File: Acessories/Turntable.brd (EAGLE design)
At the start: 80 x 50 mm, 28 parts, among them J1 HEADER4, M1 ARDUINO-NANO-3.0, U2 A4988, X1 MKDSN1,5/4-5,08

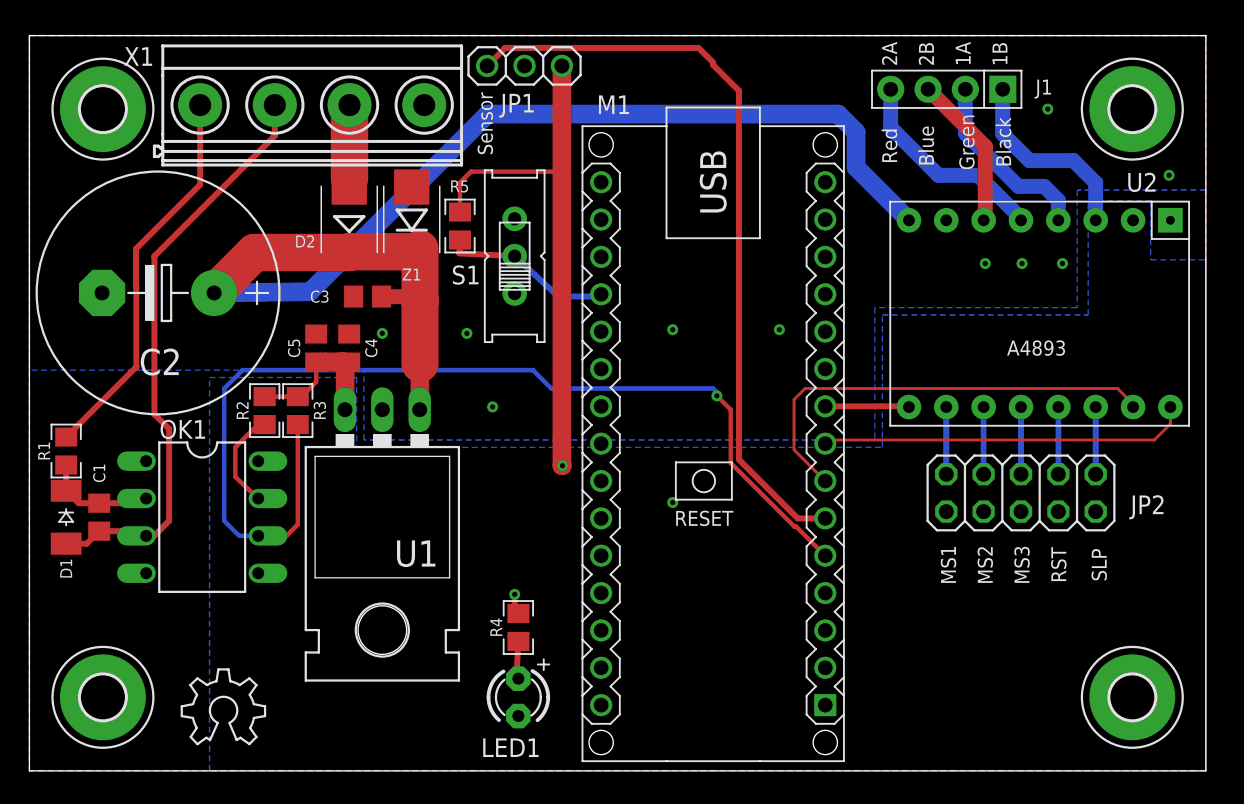
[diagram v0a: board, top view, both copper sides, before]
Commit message: Add files via upload
Added 12V regulator, Address label
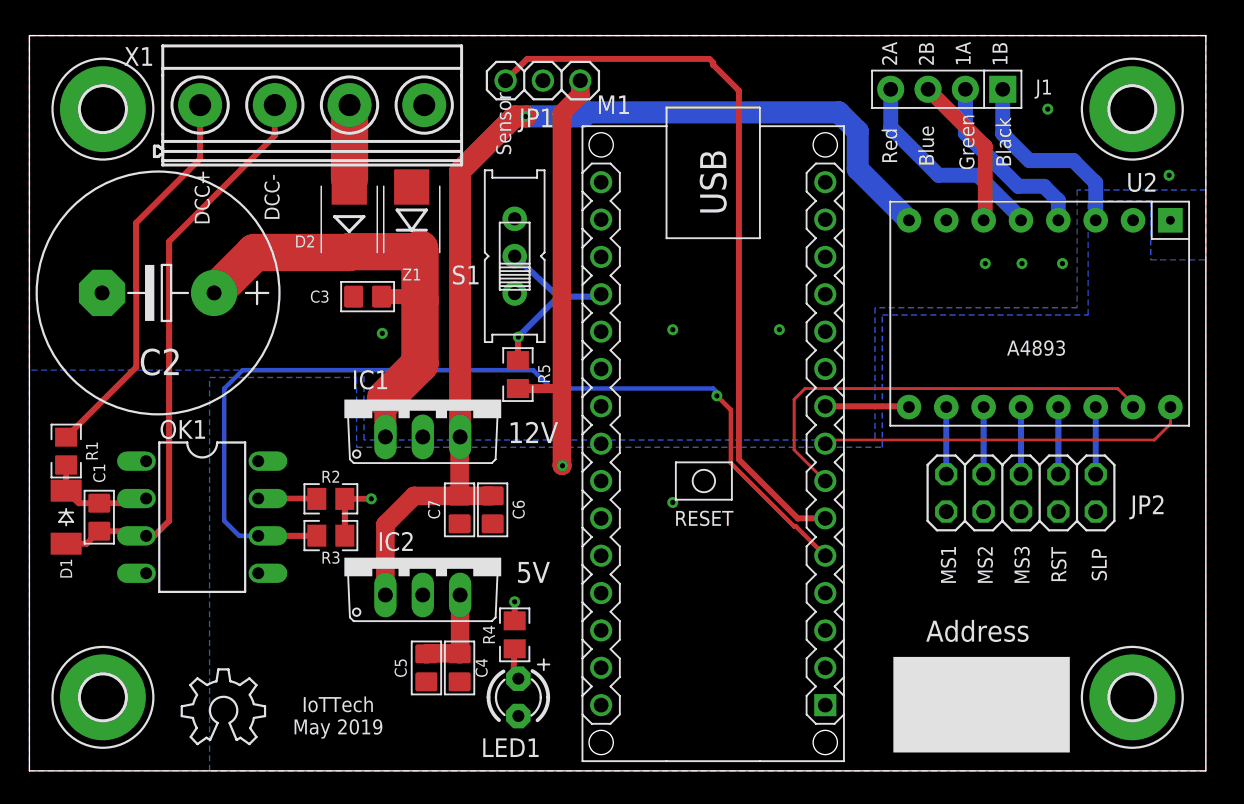
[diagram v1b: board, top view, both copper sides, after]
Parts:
- removed U1: (no value), SparkFun-IC-Power:TO-220-ALT
- added C6: 10uF, GJR:0805
- added C7: 0.1uF, GJR:0805
- added IC1: 7812TV, linear:TO220V
- added IC2: 7805TV, linear:TO220V
- C1, C3, C4, C5: device rcl:C0805 -> GJR:0805
- moved C4 23.0 mm to (-10.8, -18.0), turned to 270 degrees
- moved C5 23.0 mm to (-13.0, -18.0), turned to 270 degrees
- moved R5 10.8 mm to (-6.78, 1.95), turned to 270 degrees
- moved R3 8.79 mm to (-19.5, -9.00), turned to 0 degrees
- moved R2 7.50 mm to (-19.5, -6.50), turned to 0 degrees
- moved JP1 1.60 mm to (-5.08, 21.9)
- moved R4 0.56 mm to (-7.00, -15.8)
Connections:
- new net +12V: C6.1, C7.1, IC1.3, IC2.1, U2.8
- net +15V: now also IC1.1; no longer U1.IN, U2.8
- net +5V: now also IC2.3; no longer U1.OUT
- net GND: now also C6.2, C7.2, IC1.2, IC2.2; no longer U1.GND
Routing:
- net +12V: track 0.00 -> 71.7 mm, vias 0 -> 1
- net +15V: track 84.9 -> 31.7 mm
- net +5V: track 49.2 -> 41.9 mm, vias 2 -> 3
- net DCCIN: track 70.4 -> 64.6 mm
- net N$4: track 6.80 -> 4.00 mm
- net POS: track 51.5 -> 50.1 mm
- net TRACK2: track 40.0 -> 39.1 mm
- net LEARN: track 11.7 -> 12.5 mm, vias 0 -> 1
- net N$1: track 5.02 -> 5.58 mm
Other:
- board text added: "12V"
- board text added: "5V"
- board text added: "Address"
- board text added: "DCC+"
- board text added: "DCC-"
- board text added: "IoTTech May 2019"

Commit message: Add files via upload
Minor tweaks
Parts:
- moved R4 0.25 mm to (-6.75, -15.8)
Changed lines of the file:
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@@
 <wire x1="40" y1="25" x2="-40" y2="25" width="0" layer="20"/>
 <wire x1="-40" y1="25" x2="-40" y2="-25" width="0" layer="20"/>
-<text x="-7.75" y="19" size="1.016" layer="21" rot="R90" align="center">Sensor</text>
+<text x="-9.75" y="22" size="1.016" layer="21" rot="R90" align="center">Sensor</text>
 <text x="18.5" y="23.75" size="1.016" layer="21" rot="R90" align="center">2A</text>
 <text x="21" y="23.75" size="1.016" layer="21" rot="R90" align="center">2B</text>
@@
 <attribute name="VALUE" x="-19.5" y="-10.5" size="0.8128" layer="27" align="center"/>
 </element>
-<element name="R4" library="rcl" package="R0805" value="470R" x="-7" y="-15.75" smashed="yes" rot="R90">
-<attribute name="NAME" x="-8.75" y="-15.75" size="0.8128" layer="25" rot="R90" align="center"/>
-<attribute name="VALUE" x="-5.5" y="-15.75" size="0.6096" layer="27" rot="R90" align="center"/>
+<element name="R4" library="rcl" package="R0805" value="470R" x="-6.75" y="-15.75" smashed="yes" rot="R90">
+<attribute name="NAME" x="-8.5" y="-15.75" size="0.8128" layer="25" rot="R90" align="center"/>
+<attribute name="VALUE" x="-5.25" y="-15.75" size="0.6096" layer="27" rot="R90" align="center"/>
 </element>
 <element name="R1" library="rcl" package="R0805" value="1K" x="-37.5" y="-3.25" smashed="yes" rot="R90">
@@
 <vertex x="-40" y="2.25"/>
 </polygon>
-<via x="-8.5" y="-0.25" extent="1-16" drill="0.35"/>
+<via x="-6.75" y="-1" extent="1-16" drill="0.35"/>
 <via x="3.75" y="5" extent="1-16" drill="0.35"/>
 <via x="11" y="5" extent="1-16" drill="0.35"/>
@@
 <vertex x="-27.75" y="-25"/>
 </polygon>
-<wire x1="-7" y1="-13.5" x2="-7" y2="-14.8" width="0.4064" layer="1"/>
-<via x="-7" y="-13.5" extent="1-16" drill="0.35"/>
+<wire x1="-6.75" y1="-13.5" x2="-6.75" y2="-14.8" width="0.4064" layer="1"/>
+<via x="-6.75" y="-13.5" extent="1-16" drill="0.35"/>
 <wire x1="-3.75" y1="-4" x2="-3.75" y2="-4.25" width="0.4064" layer="1"/>
 <via x="-3.75" y="-4.25" extent="1-16" drill="0.35"/>
@@
 <contactref element="R4" pad="1"/>
 <contactref element="LED1" pad="A"/>
-<wire x1="-6.75" y1="-18.73" x2="-7.096403125" y2="-18.516828125" width="0.4064" layer="1"/>
-<wire x1="-7.096403125" y1="-18.516828125" x2="-7" y2="-16.7" width="0.4064" layer="1"/>
+<wire x1="-6.75" y1="-18.73" x2="-6.75" y2="-16.7" width="0.4064" layer="1"/>
 </signal>
 <signal name="+15V">

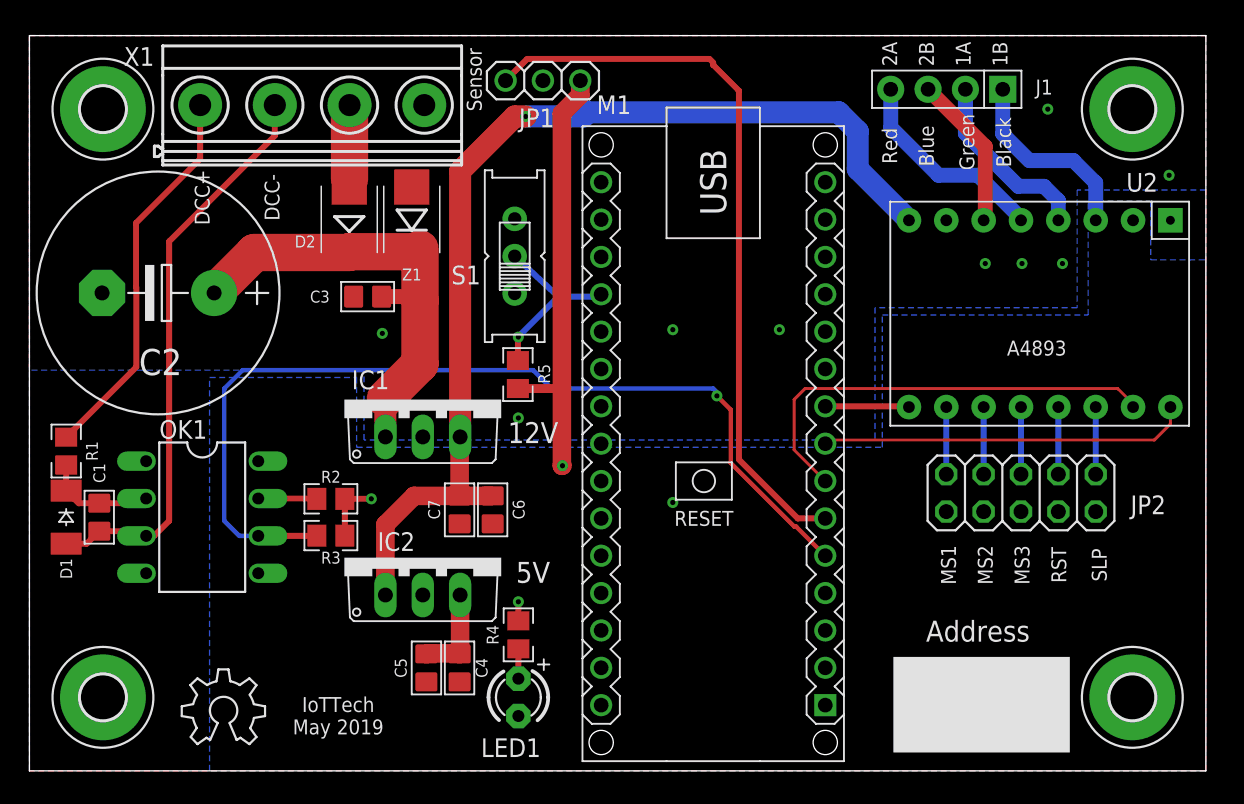
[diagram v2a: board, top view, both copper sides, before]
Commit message: Add files via upload
Added GPIO control of the stepper motor board settings, updated Peco turntable build instructions.
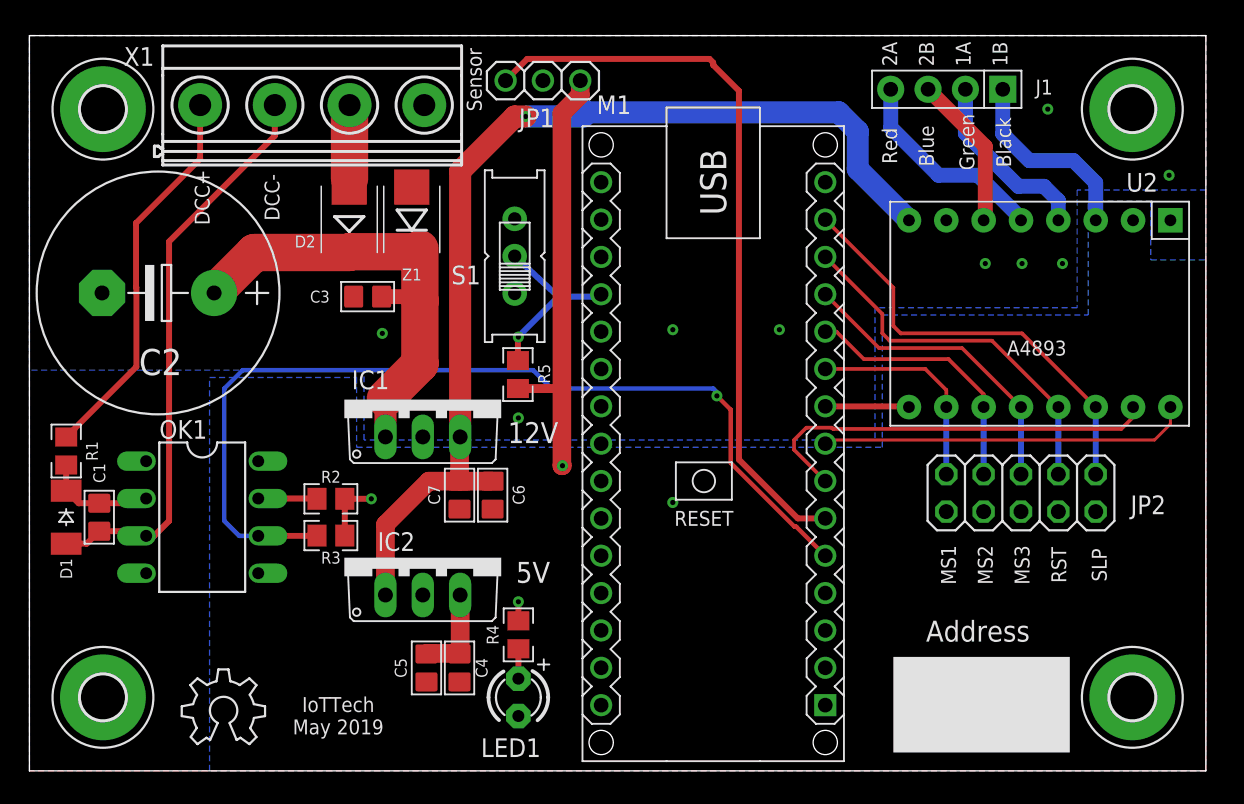
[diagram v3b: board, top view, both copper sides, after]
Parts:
- moved C6 1.00 mm to (-8.50, -6.25)
- moved C7 1.00 mm to (-10.8, -6.25)
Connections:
- net BLACK renamed 1B
- net BLUE renamed 2B
- net GREEN renamed 1A
- net RED renamed 2A
- removed net N$11: JP2.9, U2.10
- removed net N$12: JP2.1, U2.14
- removed net N$13: JP2.3, U2.13
- removed net N$14: JP2.5, U2.12
- removed net N$15: JP2.7, U2.11
- new net !RESET: JP2.3, M1.J1.13, U2.13
- new net !SLEEP: JP2.1, M1.J1.14, U2.14
- new net MS1: JP2.9, M1.J1.10, U2.10
- new net MS2: JP2.7, M1.J1.11, U2.11
- new net MS3: JP2.5, M1.J1.12, U2.12
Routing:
- net !SLEEP: track 0.00 -> 29.8 mm
- net !RESET: track 0.00 -> 25.4 mm
- net MS3: track 0.00 -> 21.1 mm
- net MS2: track 0.00 -> 18.0 mm
- net MS1: track 0.00 -> 14.6 mm
- net N$15: track 4.57 -> 0.00 mm
- net N$14: track 4.57 -> 0.00 mm
- net N$13: track 4.57 -> 0.00 mm
- net N$12: track 4.57 -> 0.00 mm
- net N$11: track 4.57 -> 0.00 mm
- net STEP: track 30.4 -> 28.1 mm
- net +12V: track 71.7 -> 71.1 mm
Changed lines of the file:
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@@
 <attribute name="VALUE" x="-8.28" y="1.95" size="0.6096" layer="27" rot="R270" align="center"/>
 </element>
-<element name="C6" library="GJR" package="0805" value="10uF" x="-8.5" y="-7.25" smashed="yes" rot="R270">
-<attribute name="FARNELL" value="" x="-8.5" y="-7.25" size="1.778" layer="27" rot="R270" display="off"/>
-<attribute name="MANUFACTURER" value="" x="-8.5" y="-7.25" size="1.778" layer="27" rot="R270" display="off"/>
-<attribute name="NAME" x="-6.73" y="-7.23" size="0.8128" layer="25" rot="R270" align="center"/>
-<attribute name="PARTNUMBER" value="" x="-8.5" y="-7.25" size="1.778" layer="27" rot="R270" display="off"/>
-<attribute name="VALUE" x="-11.04" y="-5.98" size="1.27" layer="27" rot="R270"/>
-</element>
-<element name="C7" library="GJR" package="0805" value="0.1uF" x="-10.75" y="-7.25" smashed="yes" rot="R270">
-<attribute name="FARNELL" value="" x="-10.75" y="-7.25" size="1.778" layer="27" rot="R270" display="off"/>
-<attribute name="MANUFACTURER" value="" x="-10.75" y="-7.25" size="1.778" layer="27" rot="R270" display="off"/>
-<attribute name="NAME" x="-12.48" y="-7.23" size="0.8128" layer="25" rot="R270" align="center"/>
-<attribute name="PARTNUMBER" value="" x="-10.75" y="-7.25" size="1.778" layer="27" rot="R270" display="off"/>
-<attribute name="VALUE" x="-13.29" y="-5.98" size="1.27" layer="27" rot="R270"/>
+<element name="C6" library="GJR" package="0805" value="10uF" x="-8.5" y="-6.25" smashed="yes" rot="R270">
+<attribute name="FARNELL" value="" x="-8.5" y="-6.25" size="1.778" layer="27" rot="R270" display="off"/>
+<attribute name="MANUFACTURER" value="" x="-8.5" y="-6.25" size="1.778" layer="27" rot="R270" display="off"/>
+<attribute name="NAME" x="-6.73" y="-6.23" size="0.8128" layer="25" rot="R270" align="center"/>
+<attribute name="PARTNUMBER" value="" x="-8.5" y="-6.25" size="1.778" layer="27" rot="R270" display="off"/>
+<attribute name="VALUE" x="-11.04" y="-4.98" size="1.27" layer="27" rot="R270"/>
+</element>
+<element name="C7" library="GJR" package="0805" value="0.1uF" x="-10.75" y="-6.25" smashed="yes" rot="R270">
+<attribute name="FARNELL" value="" x="-10.75" y="-6.25" size="1.778" layer="27" rot="R270" display="off"/>
+<attribute name="MANUFACTURER" value="" x="-10.75" y="-6.25" size="1.778" layer="27" rot="R270" display="off"/>
+<attribute name="NAME" x="-12.48" y="-6.23" size="0.8128" layer="25" rot="R270" align="center"/>
+<attribute name="PARTNUMBER" value="" x="-10.75" y="-6.25" size="1.778" layer="27" rot="R270" display="off"/>
+<attribute name="VALUE" x="-13.29" y="-4.98" size="1.27" layer="27" rot="R270"/>
 </element>
 <element name="IC1" library="linear" library_urn="urn:adsk.eagle:library:262" package="TO220V" package3d_urn="urn:adsk.eagle:package:16417/2" value="7812TV" x="-13.25" y="0.25" smashed="yes">
@@
 <wire x1="-18.2311" y1="14.7189" x2="-18.2311" y2="15.25" width="1.016" layer="1"/>
 </signal>
-<signal name="BLACK">
+<signal name="1B">
 <contactref element="U2" pad="3"/>
 <contactref element="J1" pad="1"/>
@@
 <wire x1="26.19" y1="18.31" x2="28" y2="16.5" width="1.016" layer="16"/>
 </signal>
-<signal name="GREEN">
+<signal name="1A">
 <contactref element="U2" pad="4"/>
 <contactref element="J1" pad="2"/>
@@
 <wire x1="23.65" y1="21.35" x2="23.65" y2="18.35" width="1.016" layer="16"/>
 </signal>
-<signal name="RED">
+<signal name="2A">
 <contactref element="U2" pad="5"/>
 <contactref element="J1" pad="4"/>
@@
 <wire x1="27.43" y1="12.57" x2="27.43" y2="12.44" width="1.016" layer="16"/>
 </signal>
-<signal name="BLUE">
+<signal name="2B">
 <contactref element="U2" pad="6"/>
 <contactref element="J1" pad="3"/>
@@
 <contactref element="M1" pad="J1.7"/>
 <contactref element="U2" pad="15"/>
-<wire x1="14.12" y1="-5.29" x2="12" y2="-3.17" width="0.2032" layer="1"/>
-<wire x1="12" y1="-3.17" x2="12" y2="0.25" width="0.2032" layer="1"/>
-<wire x1="12" y1="0.25" x2="12.75" y2="1" width="0.2032" layer="1"/>
-<wire x1="12.75" y1="1" x2="34" y2="1" width="0.2032" layer="1"/>
-<wire x1="34" y1="1" x2="35.05" y2="-0.05" width="0.2032" layer="1"/>
-<wire x1="35.05" y1="-0.05" x2="35.05" y2="-0.26" width="0.2032" layer="1"/>
+<wire x1="14.12" y1="-5.29" x2="12" y2="-3.17" width="0.254" layer="1"/>
+<wire x1="12" y1="-3.17" x2="12" y2="-2.5" width="0.254" layer="1"/>
+<wire x1="14.56909375" y1="-1.6658" x2="14.65329375" y2="-1.75" width="0.254" layer="1"/>
+<wire x1="14.65329375" y1="-1.75" x2="34.25" y2="-1.75" width="0.254" layer="1"/>
+<wire x1="12.8342" y1="-1.6658" x2="14.56909375" y2="-1.6658" width="0.254" layer="1"/>
+<wire x1="34.25" y1="-1.75" x2="35.05" y2="-0.95" width="0.254" layer="1"/>
+<wire x1="35.05" y1="-0.95" x2="35.05" y2="-0.26" width="0.254" layer="1"/>
+<wire x1="12" y1="-2.5" x2="12.8342" y2="-1.6658" width="0.254" layer="1"/>
 </signal>
 <signal name="DIR">
@@
 <wire x1="14.37" y1="-2.5" x2="36.5" y2="-2.5" width="0.2032" layer="1"/>
 <wire x1="36.5" y1="-2.5" x2="37.59" y2="-1.41" width="0.2032" layer="1"/>
-</signal>
-<signal name="N$11">
-<contactref element="U2" pad="10"/>
-<contactref element="JP2" pad="9"/>
-<wire x1="22.35" y1="-4.83" x2="22.35" y2="-0.26" width="0.4064" layer="16"/>
-</signal>
-<signal name="N$12">
-<contactref element="JP2" pad="1"/>
-<contactref element="U2" pad="14"/>
-<wire x1="32.51" y1="-4.83" x2="32.51" y2="-0.26" width="0.4064" layer="16"/>
-</signal>
-<signal name="N$13">
-<contactref element="U2" pad="13"/>
-<contactref element="JP2" pad="3"/>
-<wire x1="29.97" y1="-4.83" x2="29.97" y2="-0.26" width="0.4064" layer="16"/>
-</signal>
-<signal name="N$14">
-<contactref element="U2" pad="12"/>
-<contactref element="JP2" pad="5"/>
-<wire x1="27.43" y1="-4.83" x2="27.43" y2="-0.26" width="0.4064" layer="16"/>
-</signal>
-<signal name="N$15">
-<contactref element="U2" pad="11"/>
-<contactref element="JP2" pad="7"/>
-<wire x1="24.89" y1="-4.83" x2="24.89" y2="-0.26" width="0.4064" layer="16"/>
 </signal>
 <signal name="LEARN">
@@
 <contactref element="IC2" pad="1"/>
 <wire x1="-10.71" y1="-2.29" x2="-10.75" y2="-2.33" width="1.27" layer="1"/>
-<wire x1="-10.75" y1="-2.33" x2="-10.75" y2="-6.3" width="1.27" layer="1"/>
-<wire x1="-10.75" y1="-6.3" x2="-8.5" y2="-6.3" width="1.27" layer="1"/>
+<wire x1="-10.75" y1="-2.33" x2="-10.75" y2="-5.3" width="1.27" layer="1"/>
+<wire x1="-8.5" y1="-5.3" x2="-10.75" y2="-5.3" width="1.27" layer="1"/>
 <wire x1="-15.79" y1="-13.04" x2="-15.79" y2="-8.25" width="1.27" layer="1"/>
-<wire x1="-15.79" y1="-8.25" x2="-13.84" y2="-6.3" width="1.27" layer="1"/>
-<wire x1="-10.75" y1="-6.3" x2="-13.84" y2="-6.3" width="1.27" layer="1"/>
+<wire x1="-15.79" y1="-8.25" x2="-12.84" y2="-5.3" width="1.27" layer="1"/>
+<wire x1="-10.75" y1="-5.3" x2="-12.84" y2="-5.3" width="1.27" layer="1"/>
 <wire x1="-10.71" y1="15.79" x2="-7" y2="19.5" width="1.5" layer="1"/>
 <wire x1="-7" y1="19.5" x2="-6.25" y2="19.5" width="1.5" layer="1"/>
@@
 <wire x1="-10.71" y1="-2.29" x2="-10.71" y2="15.79" width="1.5" layer="1"/>
 </signal>
+<signal name="MS1">
+<contactref element="M1" pad="J1.10"/>
+<contactref element="U2" pad="10"/>
+<contactref element="JP2" pad="9"/>
+<wire x1="22.35" y1="-4.83" x2="22.35" y2="-0.26" width="0.4064" layer="16"/>
+<wire x1="14.12" y1="2.33" x2="20.92" y2="2.33" width="0.254" layer="1"/>
+<wire x1="22.35" y1="0.9" x2="22.35" y2="-0.26" width="0.254" layer="1"/>
+<wire x1="20.92" y1="2.33" x2="22.35" y2="0.9" width="0.254" layer="1"/>
+</signal>
+<signal name="MS2">
+<contactref element="M1" pad="J1.11"/>
+<contactref element="U2" pad="11"/>
+<contactref element="JP2" pad="7"/>
+<wire x1="24.89" y1="-4.83" x2="24.89" y2="-0.26" width="0.4064" layer="16"/>
+<wire x1="14.12" y1="4.87" x2="14.88" y2="4.87" width="0.254" layer="1"/>
+<wire x1="16.75" y1="3" x2="22.5" y2="3" width="0.254" layer="1"/>
+<wire x1="22.5" y1="3" x2="24.89" y2="0.61" width="0.254" layer="1"/>
+<wire x1="24.89" y1="0.61" x2="24.89" y2="-0.26" width="0.254" layer="1"/>
+<wire x1="14.88" y1="4.87" x2="16.75" y2="3" width="0.254" layer="1"/>
+</signal>
+<signal name="MS3">
+<contactref element="M1" pad="J1.12"/>
+<contactref element="U2" pad="12"/>
+<contactref element="JP2" pad="5"/>
+<wire x1="27.43" y1="-4.83" x2="27.43" y2="-0.26" width="0.4064" layer="16"/>
+<wire x1="14.12" y1="7.41" x2="17.78" y2="3.75" width="0.254" layer="1"/>
+<wire x1="23.42" y1="3.75" x2="27.43" y2="-0.26" width="0.254" layer="1"/>
+<wire x1="17.78" y1="3.75" x2="23.42" y2="3.75" width="0.254" layer="1"/>
+</signal>
+<signal name="!RESET">
+<contactref element="M1" pad="J1.13"/>
+<contactref element="U2" pad="13"/>
+<contactref element="JP2" pad="3"/>
+<wire x1="29.97" y1="-4.83" x2="29.97" y2="-0.26" width="0.4064" layer="16"/>
+<wire x1="14.12" y1="9.95" x2="18" y2="6.07" width="0.254" layer="1"/>
+<wire x1="18" y1="6.07" x2="18" y2="4.75" width="0.254" layer="1"/>
+<wire x1="18" y1="4.75" x2="18.5" y2="4.25" width="0.254" layer="1"/>
+<wire x1="25.46" y1="4.25" x2="29.97" y2="-0.26" width="0.254" layer="1"/>
+<wire x1="18.5" y1="4.25" x2="25.46" y2="4.25" width="0.254" layer="1"/>
+</signal>
+<signal name="!SLEEP">
+<contactref element="M1" pad="J1.14"/>
+<contactref element="JP2" pad="1"/>
+<contactref element="U2" pad="14"/>
+<wire x1="32.51" y1="-4.83" x2="32.51" y2="-0.26" width="0.4064" layer="16"/>
+<wire x1="14.12" y1="12.49" x2="18.75" y2="7.86" width="0.254" layer="1"/>
+<wire x1="18.75" y1="7.86" x2="18.75" y2="5.25" width="0.254" layer="1"/>
+<wire x1="18.75" y1="5.25" x2="19.25" y2="4.75" width="0.254" layer="1"/>
+<wire x1="27.5" y1="4.75" x2="32.51" y2="-0.26" width="0.254" layer="1"/>
+<wire x1="19.25" y1="4.75" x2="27.5" y2="4.75" width="0.254" layer="1"/>
+</signal>
 </signals>
